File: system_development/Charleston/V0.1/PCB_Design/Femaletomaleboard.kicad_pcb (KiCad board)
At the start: 2 copper layers, 64.4 x 118.3 mm, 7 parts, among them SW2 MC74VHC1G66DFT1G

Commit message: femaletomaleboard
Fingers crossed final version
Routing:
- net (no net): track 2812.3 -> 2811.5 mm
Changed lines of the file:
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@@
   (segment (start 142.325948 110.855) (end 142.235473 110.764525) (width 0.25) (layer "F.Cu") (net 0))
   (segment (start 144.469667 91.365) (end 144.369667 91.465) (width 0.25) (layer "F.Cu") (net 0))
-  (segment (start 167.669667 107.985) (end 167.669667 107.1) (width 0.25) (layer "F.Cu") (net 0))
   (segment (start 142.225948 116.295) (end 141.990473 116.059525) (width 0.25) (layer "F.Cu") (net 0))
   (segment (start 155.7 151.65) (end 157.4 153.35) (width 0.25) (layer "F.Cu") (net 0))

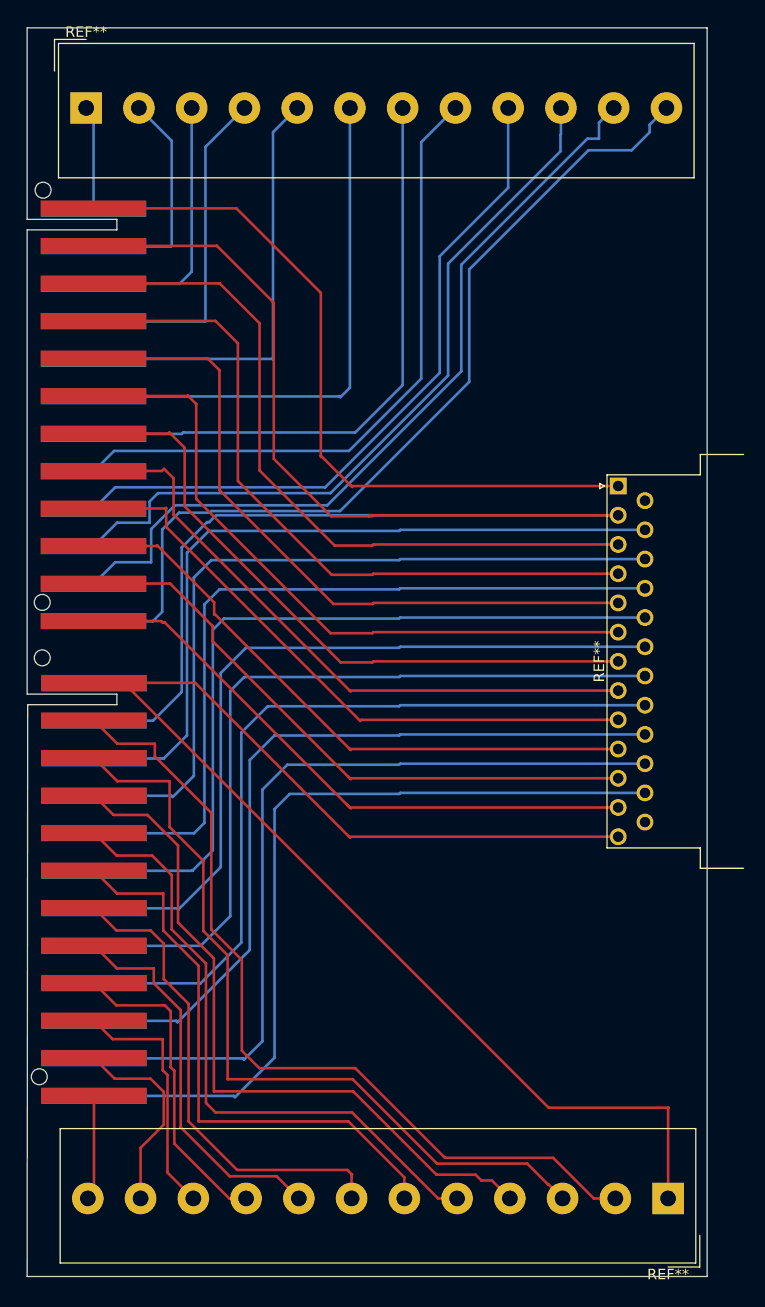
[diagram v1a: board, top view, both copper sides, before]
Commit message: Femaletomaleboard
I retracked everything and cleaned some stuff up
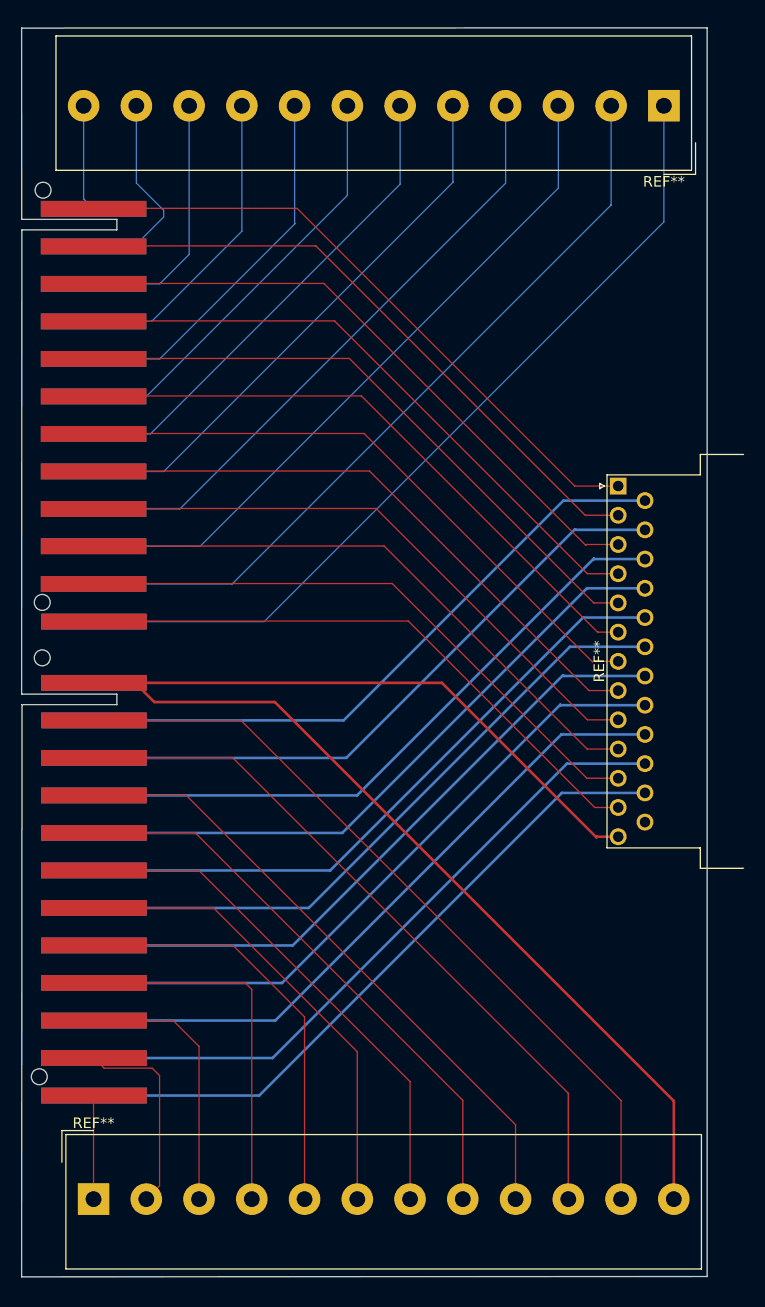
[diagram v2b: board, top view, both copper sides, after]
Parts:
- removed the SW2 at (123.5, 79.1)
- removed the SW2 at (123.6, 126.1)
- added ?: , , F.Cu at (117.9, 88.0)
- added ?: , , F.Cu at (117.9, 73.8)
- added ?: , , B.Cu at (118.0, 125.8)
- added ?: , , B.Cu at (118.0, 129.4)
- added ?: , , B.Cu at (118.0, 111.6)
- added ?: , , B.Cu at (118.0, 132.9)
- added ?: , , B.Cu at (118.0, 115.2)
- added ?: , , B.Cu at (118.0, 140.0)
- added ?: , , B.Cu at (118.0, 143.6)
- added ?: , , B.Cu at (118.0, 108.0)
- added ?: , , B.Cu at (118.0, 118.7)
- added ?: , , F.Cu at (117.9, 63.1)
- added ?: , , B.Cu at (118.0, 122.3)
- added ?: , , B.Cu at (118.0, 136.5)
- added ?: , , F.Cu at (117.9, 80.9)
- added ?: , , F.Cu at (117.9, 91.5)
- added ?: , , F.Cu at (117.9, 70.2)
- added ?: , , F.Cu at (117.9, 84.4)
- added ?: , , F.Cu at (117.9, 95.1)
- added ?: , , F.Cu at (117.9, 77.3)
- added ?: , , F.Cu at (117.9, 66.7)
- added SW2: MC74VHC1G66DFT1G, infnoise_goldfingers:Gold Finger single, F.Cu at (112.4, 40.0)
- added SW2: MC74VHC1G66DFT1G, infnoise_goldfingers:Gold Finger single, F.Cu at (112.4, 79.1)
- added SW2: MC74VHC1G66DFT1G, infnoise_goldfingers:Gold Finger single, B.Cu at (112.4, 124.0)
- moved REF** 54.8 mm to (172.0, 49.8), turned to 180 degrees
- moved REF** 54.5 mm to (117.9, 153.4), turned to 0 degrees
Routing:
- net (no net): track 2811.5 -> 2549.6 mm
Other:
- board size 64.4 x 118.3 mm -> 65 x 118.4 mm

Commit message: updates
updates
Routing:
- net (no net): track 2549.6 -> 2551.0 mm

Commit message: did it correctly with netlist and all.
Re did it with same desgin but with netlist and proper way
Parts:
- removed ? (x21): , 
- removed REF** (x2): Altech_AK300_1x12_P5.00mm_45-Degree, TerminalBlock_Altech:Altech_AK300_1x12_P5.00mm_45-Degree
- removed REF**: DSUB-25_Female_Horizontal_P2.77x2.54mm_EdgePinOffset9.40mm, Connector_Dsub:DSUB-25_Female_Horizontal_P2.77x2.54mm_EdgePinOffset9.40mm
- removed SW2: MC74VHC1G66DFT1G, infnoise_goldfingers:Gold Finger PCB
- removed SW2 (x3): MC74VHC1G66DFT1G, infnoise_goldfingers:Gold Finger single
- removed SW2: MC74VHC1G66DFT1G, infnoise_goldfingers:Gold Finger PCB bottom
- added J2: Screw_Terminal_01x12, TerminalBlock_Altech:Altech_AK300_1x12_P5.00mm_45-Degree, F.Cu at (172.0, 49.8)
- added J3: DB25_Receptacle, Connector_Dsub:DSUB-25_Female_Horizontal_P2.77x2.54mm_EdgePinOffset9.40mm, F.Cu at (161.9, 81.1)
- added J4: Screw_Terminal_01x12, TerminalBlock_Altech:Altech_AK300_1x12_P5.00mm_45-Degree, F.Cu at (117.0, 152.8)
- added U2: ~, infnoise_goldfingers:Gold Finger PCB, F.Cu at (123.3, 78.9)
- added U2: ~, infnoise_goldfingers:Gold Finger PCB, B.Cu at (112.1, 78.9)
- added U3: ~, infnoise_goldfingers:Gold Finger PCB, F.Cu at (123.3, 124.0)
- added U3: ~, infnoise_goldfingers:Gold Finger PCB, B.Cu at (112.1, 124.0)
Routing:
- net (no net): track 2551.0 -> 0.00 mm
- net Net-(J2-Pin_2): track 0.00 -> 241.7 mm
- net Net-(J3-P14): track 0.00 -> 130.8 mm
- net Net-(J2-Pin_1): track 0.00 -> 130.6 mm
- net Net-(J4-Pin_12): track 0.00 -> 128.1 mm
- net Net-(J3-P15): track 0.00 -> 123.5 mm
- net Net-(J2-Pin_3): track 0.00 -> 120.1 mm
- net Net-(J2-Pin_4): track 0.00 -> 114.2 mm
- net Net-(J3-P17): track 0.00 -> 109.9 mm
- net Net-(J2-Pin_5): track 0.00 -> 108.3 mm
- net Net-(J3-P18): track 0.00 -> 103.7 mm
- net Net-(J2-Pin_6): track 0.00 -> 102.6 mm
- net Net-(J3-P19): track 0.00 -> 99.0 mm
- net Net-(J2-Pin_7): track 0.00 -> 96.9 mm
- net Net-(J3-P20): track 0.00 -> 94.1 mm
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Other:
- outline, holes or cut-outs redrawn
